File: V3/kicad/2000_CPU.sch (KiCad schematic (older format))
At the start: 21 parts, among them U2100 Z8-L180-S180-180-PQFP-80, U2101 GAL16V8, U2102 14.7456 MHz, U2103 74HCT273

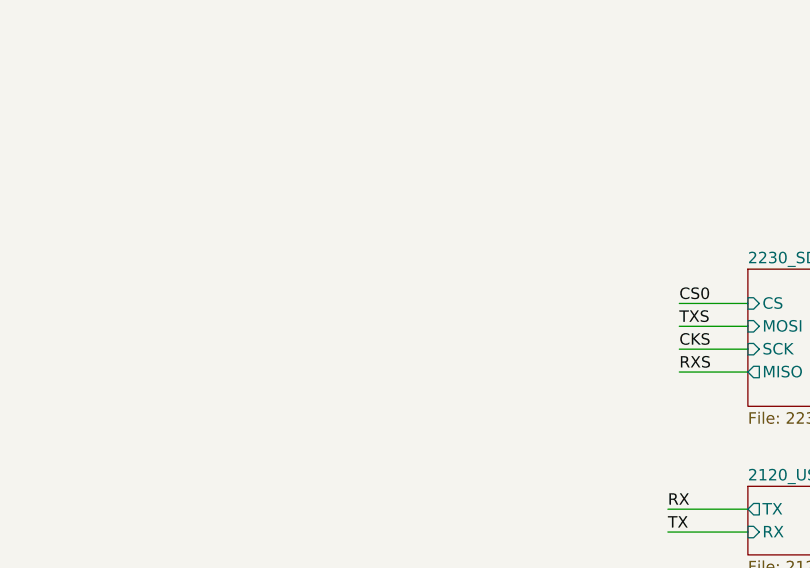
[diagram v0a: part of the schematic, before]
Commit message: Added pin header for SPI lines
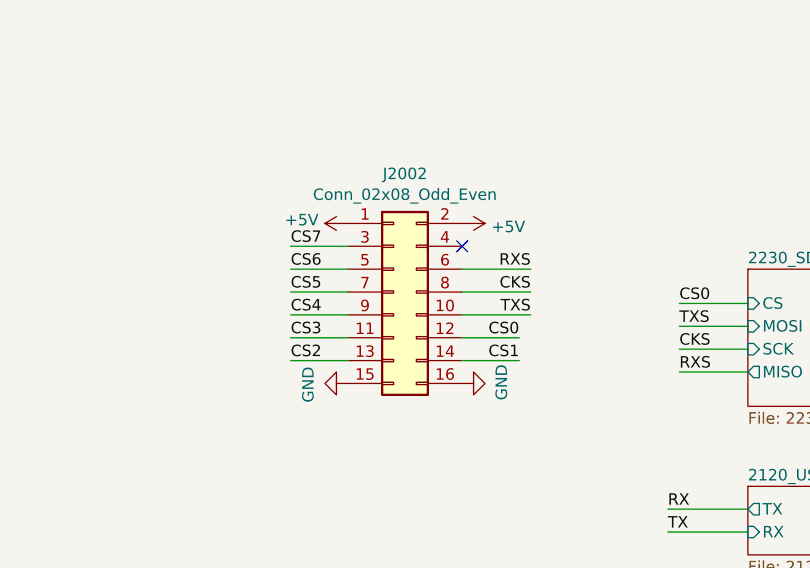
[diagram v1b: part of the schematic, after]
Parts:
- added J2002: Conn_02x08_Odd_Even, Connector_PinHeader_2.54mm:PinHeader_2x08_P2.54mm_Vertical, symbol Connector_Generic:Conn_02x08_Odd_Even
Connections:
- net +5V: now also J2002.1 (Pin_1), J2002.2 (Pin_2)
- net CKS: now also J2002.8 (Pin_8)
- net CS0: now also J2002.12 (Pin_12)
- net CS1: now also J2002.14 (Pin_14)
- net CS2: now also J2002.13 (Pin_13)
- net CS3: now also J2002.11 (Pin_11)
- net CS4: now also J2002.9 (Pin_9)
- net CS5: now also J2002.7 (Pin_7)
- net CS6: now also J2002.5 (Pin_5)
- net CS7: now also J2002.3 (Pin_3)
- net GND: now also J2002.15 (Pin_15), J2002.16 (Pin_16)
- net RXS: now also J2002.6 (Pin_6)
- net TXS: now also J2002.10 (Pin_10)
- no-connect marks 15 -> 16
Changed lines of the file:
@@
+	1    0    0    -1
+$EndComp
+Wire Wire Line
+	7250 5100 7550 5100
+Text Label 7550 5100 2    50   ~ 0
+CKS
+Wire Wire Line
+	7250 5000 7550 5000
+Text Label 7550 5000 2    50   ~ 0
+RXS
+Wire Wire Line
+	7250 5200 7550 5200
+Text Label 7550 5200 2    50   ~ 0
+TXS
+Text Label 6500 5200 0    50   ~ 0
+CS4
+Wire Wire Line
+	6500 5200 6750 5200
+Text Label 6500 5100 0    50   ~ 0
+CS5
+Wire Wire Line
+	6500 5100 6750 5100
+Text Label 6500 5000 0    50   ~ 0
+CS6
+Wire Wire Line
+	6500 5000 6750 5000
+Text Label 6500 4900 0    50   ~ 0
+CS7
+Wire Wire Line
+	6500 4900 6750 4900
+Text Label 7500 5300 2    50   ~ 0
+CS0
+Wire Wire Line
+	7500 5300 7250 5300
+Text Label 7500 5400 2    50   ~ 0
+CS1
+Wire Wire Line
+	7500 5400 7250 5400
+Text Label 6500 5400 0    50   ~ 0
+CS2
+Wire Wire Line
+	6500 5400 6750 5400
+Text Label 6500 5300 0    50   ~ 0
+CS3
+Wire Wire Line
+	6500 5300 6750 5300
+$Comp
+L power:+5V #PWR?
+U 1 1 638AF739
+P 6750 4800
+AR Path="/6191B6A2/61EBDADB/638AF739" Ref="#PWR?"  Part="1"
+AR Path="/63A83936/638AF739" Ref="#PWR0168"  Part="1"
+F 0 "#PWR0168" H 6750 4650 50  0001 C CNN
+F 1 "+5V" V 6765 4928 50  0000 L CNN
+F 2 "" H 6750 4800 50  0001 C CNN
+F 3 "" H 6750 4800 50  0001 C CNN
+	1    6750 4800
+	0    -1   -1   0
+$EndComp
+$Comp
+L power:+5V #PWR?
+U 1 1 638B5C37
+P 7250 4800
+AR Path="/6191B6A2/61EBDADB/638B5C37" Ref="#PWR?"  Part="1"
+AR Path="/63A83936/638B5C37" Ref="#PWR0169"  Part="1"
+F 0 "#PWR0169" H 7250 4650 50  0001 C CNN
+F 1 "+5V" V 7265 4928 50  0000 L CNN
+F 2 "" H 7250 4800 50  0001 C CNN
+F 3 "" H 7250 4800 50  0001 C CNN
+	1    7250 4800
+	0    1    1    0
+$EndComp
+$Comp
+L power:GND #PWR?
+U 1 1 638BC202
+P 6750 5500
+AR Path="/638BC202" Ref="#PWR?"  Part="1"
+AR Path="/62497D60/638BC202" Ref="#PWR?"  Part="1"
+AR Path="/61D852D7/638BC202" Ref="#PWR?"  Part="1"
+AR Path="/6195D2C9/638BC202" Ref="#PWR?"  Part="1"
+AR Path="/6191B6A2/61F28B7D/638BC202" Ref="#PWR?"  Part="1"
+AR Path="/6191B6A2/61EBDADB/638BC202" Ref="#PWR?"  Part="1"
+AR Path="/63A83936/638BC202" Ref="#PWR0171"  Part="1"
+F 0 "#PWR0171" H 6750 5250 50  0001 C CNN
+F 1 "GND" H 6755 5327 50  0000 C CNN
+F 2 "" H 6750 5500 50  0001 C CNN
+F 3 "" H 6750 5500 50  0001 C CNN
+	1    6750 5500
+	0    1    1    0
+$EndComp
+$Comp
+L power:GND #PWR?
+U 1 1 638C252B
+P 7250 5500
+AR Path="/638C252B" Ref="#PWR?"  Part="1"
+AR Path="/62497D60/638C252B" Ref="#PWR?"  Part="1"
+AR Path="/61D852D7/638C252B" Ref="#PWR?"  Part="1"
+AR Path="/6195D2C9/638C252B" Ref="#PWR?"  Part="1"
+AR Path="/6191B6A2/61F28B7D/638C252B" Ref="#PWR?"  Part="1"
+AR Path="/6191B6A2/61EBDADB/638C252B" Ref="#PWR?"  Part="1"
+AR Path="/63A83936/638C252B" Ref="#PWR0172"  Part="1"
+F 0 "#PWR0172" H 7250 5250 50  0001 C CNN
+F 1 "GND" H 7255 5327 50  0000 C CNN
+F 2 "" H 7250 5500 50  0001 C CNN
+F 3 "" H 7250 5500 50  0001 C CNN
+	1    7250 5500
+	0    -1   -1   0
+$EndComp
+NoConn ~ 7250 4900
+$Comp
+L Connector_Generic:Conn_02x08_Odd_Even J2002
+U 1 1 638D8A05
+P 6950 5100
+F 0 "J2002" H 7000 5617 50  0000 C CNN
+F 1 "Conn_02x08_Odd_Even" H 7000 5526 50  0000 C CNN
+F 2 "Connector_PinHeader_2.54mm:PinHeader_2x08_P2.54mm_Vertical" H 6950 5100 50  0001 C CNN
+F 3 "~" H 6950 5100 50  0001 C CNN
+	1    6950 5100
 	1    0    0    -1
 $EndComp

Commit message: CTS0 no longer drives an LED
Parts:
- removed R12: R, Resistor_SMD:R_1206_3216Metric, symbol Device:R
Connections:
- net CTS0: now also U2101.6 (I6)
- no-connect marks 16 -> 15
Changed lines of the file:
@@
 CTS0
 Wire Wire Line
-	9750 4500 9450 4500
-Text Label 9450 4500 0    50   ~ 0
+	1650 6750 1350 6750
+Text Label 1350 6750 0    50   ~ 0
 CTS0
 Wire Wire Line
@@
 	0    1    1    0
 $EndComp
-$Comp
-L Device:R R12
-U 1 1 62F0767B
-P 9900 4500
-AR Path="/6191B6A2/61EBDADB/62F0767B" Ref="R12"  Part="1"
-AR Path="/63A83936/62F0767B" Ref="R2006"  Part="1"
-F 0 "R2006" V 9693 4500 50  0000 C CNN
-F 1 "R" V 9784 4500 50  0000 C CNN
-F 2 "Resistor_SMD:R_1206_3216Metric" V 9830 4500 50  0001 C CNN
-F 3 "~" H 9900 4500 50  0001 C CNN
-	1    9900 4500
-	0    1    1    0
-$EndComp
-$Comp
-L power:+5V #PWR0140
-U 1 1 62F07681
-P 10050 4500
-AR Path="/6191B6A2/61EBDADB/62F07681" Ref="#PWR0140"  Part="1"
-AR Path="/63A83936/62F07681" Ref="#PWR0136"  Part="1"
-F 0 "#PWR0136" H 10050 4350 50  0001 C CNN
-F 1 "+5V" V 10065 4628 50  0000 L CNN
-F 2 "" H 10050 4500 50  0001 C CNN
-F 3 "" H 10050 4500 50  0001 C CNN
-	1    10050 4500
-	0    1    1    0
-$EndComp
 Wire Wire Line
 	4150 3100 4450 3100
@@
 Text HLabel 4450 2800 2    50   Output ~ 0
 WR
-NoConn ~ 1650 6750
 NoConn ~ 1650 6850
 NoConn ~ 1650 6950

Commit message: got CTS0 and RTS mixed up
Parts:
- removed D2103/RTS1: LED, LED_THT:LED_D3.0mm, symbol Device:LED
- removed R17: R, Resistor_SMD:R_1206_3216Metric, symbol Device:R
- added R2006: R, Resistor_SMD:R_1206_3216Metric, symbol Device:R
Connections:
- net +5V: now also R2006.1
- net CTS0: now also R2006.2; no longer U2101.6 (I6)
- net RTS0: now also U2101.6 (I6)
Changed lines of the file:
@@
-CTS0
-Wire Wire Line
-	1650 6750 1350 6750
-Text Label 1350 6750 0    50   ~ 0
 CTS0
 Wire Wire Line
@@
 Wire Wire Line
 	1700 4650 2000 4650
-Text Label 9200 2250 0    50   ~ 0
-RTS0
-Wire Wire Line
-	9450 2250 9200 2250
-$Comp
-L Device:LED D2103/RTS1
-U 1 1 62EF4C51
-P 9600 2250
-AR Path="/6191B6A2/61EBDADB/62EF4C51" Ref="D2103/RTS1"  Part="1"
-AR Path="/63A83936/62EF4C51" Ref="D2003/RTS1"  Part="1"
-F 0 "D2003/RTS1" H 9450 2400 50  0000 C TNN
-F 1 "LED" H 9600 2150 50  0000 C CNN
-F 2 "LED_THT:LED_D3.0mm" H 9600 2250 50  0001 C CNN
-F 3 "~" H 9600 2250 50  0001 C CNN
-	1    9600 2250
-	1    0    0    -1
-$EndComp
-$Comp
-L Device:R R17
-U 1 1 62EF4C59
-P 9900 2250
-AR Path="/6191B6A2/61EBDADB/62EF4C59" Ref="R17"  Part="1"
-AR Path="/63A83936/62EF4C59" Ref="R2003"  Part="1"
-F 0 "R2003" V 9693 2250 50  0000 C CNN
-F 1 "R" V 9784 2250 50  0000 C CNN
-F 2 "Resistor_SMD:R_1206_3216Metric" V 9830 2250 50  0001 C CNN
-F 3 "~" H 9900 2250 50  0001 C CNN
-	1    9900 2250
-	0    1    1    0
-$EndComp
 NoConn ~ 1650 6250
 $Comp
@@
 	1    9600 2650
 	1    0    0    -1
-$EndComp
-$Comp
-L power:+5V #PWR0107
-U 1 1 62F15912
-P 10050 2250
-AR Path="/6191B6A2/61EBDADB/62F15912" Ref="#PWR0107"  Part="1"
-AR Path="/63A83936/62F15912" Ref="#PWR0137"  Part="1"
-F 0 "#PWR0137" H 10050 2100 50  0001 C CNN
-F 1 "+5V" V 10065 2378 50  0000 L CNN
-F 2 "" H 10050 2250 50  0001 C CNN
-F 3 "" H 10050 2250 50  0001 C CNN
-	1    10050 2250
-	0    1    1    0
 $EndComp
 $Comp
@@
 	1    0    0    -1
 $EndComp
+$Comp
+L Device:R R?
+U 1 1 63AA26E6
+P 9900 4500
+AR Path="/6191B6A2/61EBDADB/63AA26E6" Ref="R?"  Part="1"
+AR Path="/63A83936/63AA26E6" Ref="R2006"  Part="1"
+F 0 "R2006" V 9693 4500 50  0000 C CNN
+F 1 "R" V 9784 4500 50  0000 C CNN
+F 2 "Resistor_SMD:R_1206_3216Metric" V 9830 4500 50  0001 C CNN
+F 3 "~" H 9900 4500 50  0001 C CNN
+	1    9900 4500
+	0    1    1    0
+$EndComp
+$Comp
+L power:+5V #PWR?
+U 1 1 63AA26EC
+P 10050 4500
+AR Path="/6191B6A2/61EBDADB/63AA26EC" Ref="#PWR?"  Part="1"
+AR Path="/63A83936/63AA26EC" Ref="#PWR?"  Part="1"
+F 0 "#PWR?" H 10050 4350 50  0001 C CNN
+F 1 "+5V" V 10065 4628 50  0000 L CNN
+F 2 "" H 10050 4500 50  0001 C CNN
+F 3 "" H 10050 4500 50  0001 C CNN
+	1    10050 4500
+	0    1    1    0
+$EndComp
+Wire Wire Line
+	9750 4500 9450 4500
+Text Label 9450 4500 0    50   ~ 0
+CTS0
+Text Label 1400 6750 0    50   ~ 0
+RTS0
+Wire Wire Line
+	1650 6750 1400 6750
 Wire Bus Line
 	1700 3150 1700 3850
